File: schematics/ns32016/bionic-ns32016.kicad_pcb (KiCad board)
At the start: 2 copper layers, 66 x 71.1 mm, 17 parts, among them J1 Bionic-P135, J2 Bionic-P245, U1 NS32016N, U2 74HCT126, U3 74HCT541, U4 74HCT541, U5 11AA010-I/TO

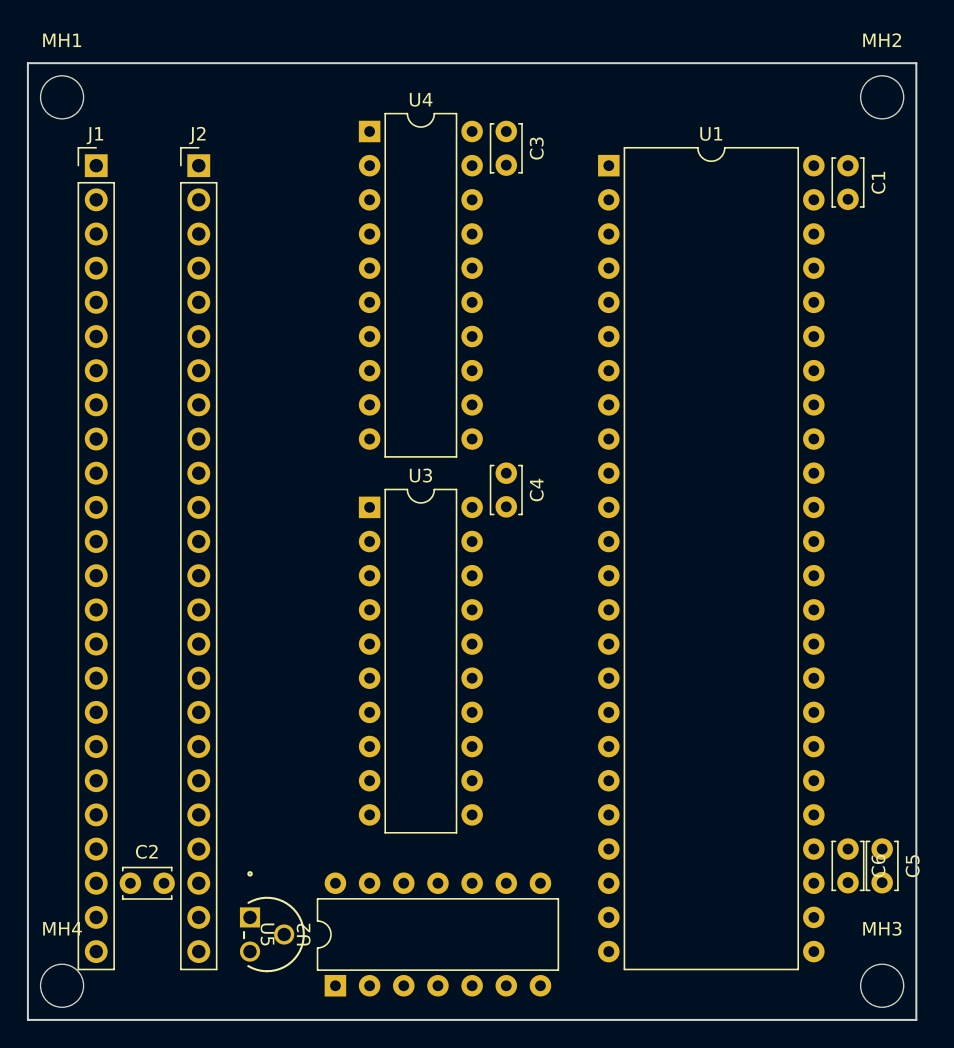
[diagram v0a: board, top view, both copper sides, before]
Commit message: [WIP] [NS32016] Update schematics
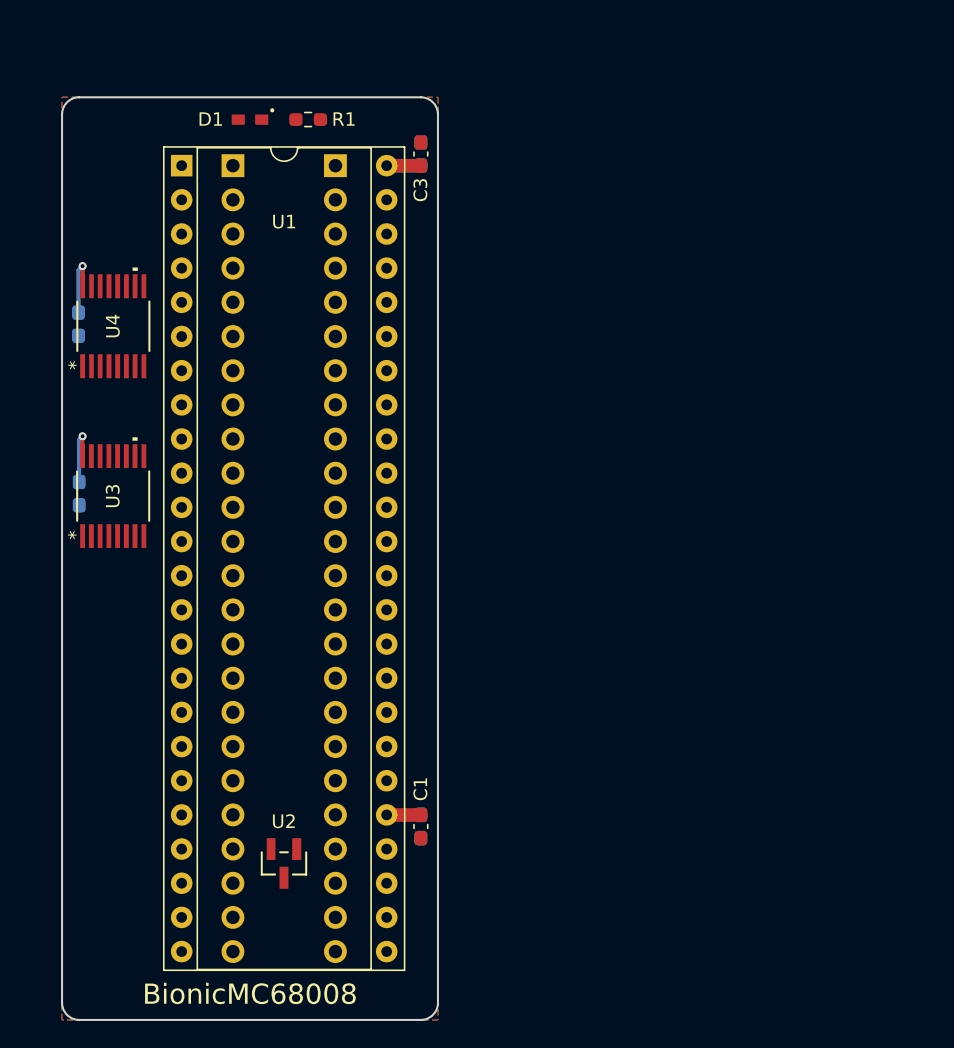
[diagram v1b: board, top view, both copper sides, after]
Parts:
- removed MH1, MH2, MH3, MH4: MountingHole_3.2mm_M3, MountingHole:MountingHole_3.2mm_M3
- removed U5: 11AA010-I/TO, microchip:TO-92_MC_MCH
- added D1: CSL1901UW1, rhom:LED_CSL1901UW1_ROM-M, F.Cu at (115.0, 71.7)
- added R1: 1.6k, Resistor_SMD:R_0603_1608Metric_Pad0.98x0.95mm_HandSolder, F.Cu at (119.3, 71.7)
- C1: value 0.1u -> 1u; footprint Capacitor_THT:C_Disc_D3.4mm_W2.1mm_P2.50mm -> Capacitor_SMD:C_0603_1608Metric_Pad1.08x0.95mm_HandSolder
- C2: value 0.1u -> 1n; footprint Capacitor_THT:C_Disc_D3.4mm_W2.1mm_P2.50mm -> Capacitor_SMD:C_0603_1608Metric_Pad1.08x0.95mm_HandSolder; moved to B.Cu
- C3: footprint Capacitor_THT:C_Disc_D3.4mm_W2.1mm_P2.50mm -> Capacitor_SMD:C_0603_1608Metric_Pad1.08x0.95mm_HandSolder
- C4: value 0.1u -> 22u; footprint Capacitor_THT:C_Disc_D3.4mm_W2.1mm_P2.50mm -> Capacitor_SMD:C_0603_1608Metric_Pad1.08x0.95mm_HandSolder; moved to B.Cu
- C5: value 1000p -> 0.1u; footprint Capacitor_THT:C_Disc_D3.4mm_W2.1mm_P2.50mm -> Capacitor_SMD:C_0603_1608Metric_Pad1.08x0.95mm_HandSolder; moved to B.Cu
- C6: value 1u -> 0.1u; footprint Capacitor_THT:C_Disc_D3.4mm_W2.1mm_P2.50mm -> Capacitor_SMD:C_0603_1608Metric_Pad1.08x0.95mm_HandSolder; moved to B.Cu
- J1: footprint connector:Bionic-P135_Vertical -> bionic:Bionic-P135_Vertical; moved to B.Cu
- J2: footprint connector:Bionic-P245_Vertical -> bionic:Bionic-P245_Vertical; moved to B.Cu
- U1: footprint Package_DIP:DIP-48_W15.24mm -> bionic:DIP-48_W15.24mm_Socket
- U2: value 74HCT126 -> 11AA010-I/TT; footprint Package_DIP:DIP-14_W7.62mm -> microchip:SOT-23_MC_MCH-M
- U3, U4: value 74HCT541 -> 74AHCT157; footprint Package_DIP:DIP-20_W7.62mm -> ti:PW16-M
- moved C6 69.2 mm to (102.2, 86.9)
- moved C5 65.3 mm to (102.3, 99.5)
- moved C1 58.5 mm to (127.7, 124.2)
- moved U1 31.7 mm to (109.9, 75.1)
- moved C4 24.6 mm to (127.7, 74.2), turned to 90 degrees
- moved U4 23.9 mm to (104.8, 87.0), turned to 90 degrees
- moved C2 22.0 mm to (127.7, 124.2), turned to -90 degrees
- moved U3 19.1 mm to (104.8, 99.6), turned to 90 degrees
- moved J1 10.2 mm to (113.7, 75.1), turned to 180 degrees
- moved J2 10.2 mm to (121.3, 75.1), turned to 180 degrees
- moved U2 9.87 mm to (117.5, 126.9), turned to 180 degrees
- moved C3 6.57 mm to (127.7, 74.2), turned to 90 degrees
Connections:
- C1 pad 1: VCC -> Net-(U1-BBG)
- C2 pad 1: VCC -> Net-(U1-BBG)
- C5 pad 1: Net-(U1-BBG) -> VCC
- C6 pad 1: Net-(U1-BBG) -> VCC
- U1 pad 1: Net-(U1-A22) -> /A22
- U1 pad 2: Net-(U1-A21) -> /A21
- U1 pad 26: Net-(U1-PHI1) -> /P46
- U1 pad 27: Net-(U1-PHI2) -> /P47
- U1 pad 3: Net-(U1-A20) -> /A20
- U1 pad 30: /P41 -> /P55
- U1 pad 31: /P45 -> /P54
- U1 pad 32: Net-(U1-~{HBE}) -> /P43
- U1 pad 33: /P50 -> /P41
- U1 pad 36: Net-(U1-U/~{S}) -> /ST4
- U1 pad 38: Net-(U1-~{DDIN}) -> /P42
- U1 pad 39: /P51 -> /ST6
- U1 pad 4: Net-(U1-A19) -> /A19
- U1 pad 40: Net-(U1-ST3) -> /ST3
- U1 pad 41: Net-(U1-ST2) -> /ST2
- U1 pad 42: Net-(U1-ST1) -> /ST1
- U1 pad 43: Net-(U1-ST0) -> /ST0
- U1 pad 44: Net-(U1-~{ILO}) -> /ST5
- U1 pad 45: /P43 -> /P51
- U1 pad 46: /P42 -> /P50
- U1 pad 47: Net-(U1-A23) -> /A23
- U1 pad 5: Net-(U1-A18) -> /A18
- U1 pad 6: Net-(U1-A17) -> /A17
- U1 pad 7: Net-(U1-A16) -> /A16
- U2 pad 1: VCC -> Net-(J2-P57)
- U2 pad 2: /P47 -> VCC
- U2 pad 3: Net-(U1-PHI2) -> GND
- U3 pad 1: /P55 -> /P45
- U3 pad 10: VCC -> /ST6
- U3 pad 11: /P30 -> /A18
- U3 pad 12: /P31 -> /P30
- U3 pad 13: /P32 -> GND
- U3 pad 14: /P33 -> /A19
- U3 pad 15: /P34 -> GND
- U3 pad 16: /P35 -> VCC
- U3 pad 2: Net-(U1-A23) -> /A16
- U3 pad 3: Net-(U1-A22) -> /ST4
- U3 pad 4: Net-(U1-A21) -> /P33
- U3 pad 5: Net-(U1-A20) -> /A17
- U3 pad 6: Net-(U1-A19) -> /ST5
- U3 pad 7: Net-(U1-A18) -> /P32
- U3 pad 8: Net-(U1-A17) -> GND
- U3 pad 9: Net-(U1-A16) -> /P31
- U4 pad 1: /P54 -> /P45
- U4 pad 10: GND -> /ST2
- U4 pad 11: /P37 -> /A22
- U4 pad 12: /P36 -> /P34
- U4 pad 13: /P35 -> /ST3
- U4 pad 14: /P34 -> /A23
- U4 pad 15: /P33 -> GND
- U4 pad 16: /P32 -> VCC
- U4 pad 2: Net-(U1-ST0) -> /A20
- U4 pad 3: Net-(U1-ST1) -> /ST0
- U4 pad 4: Net-(U1-ST2) -> /P37
- U4 pad 5: Net-(U1-ST3) -> /A21
- U4 pad 6: Net-(U1-U/~{S}) -> /ST1
- U4 pad 7: Net-(U1-~{ILO}) -> /P36
- U4 pad 8: Net-(U1-~{DDIN}) -> GND
- U4 pad 9: Net-(U1-~{HBE}) -> /P35
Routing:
- net VCC: track 0.00 -> 15.1 mm, vias 0 -> 2
- net Net-(U1-BBG): track 0.00 -> 5.08 mm
- added copper zone on B.Cu, net GND
- added copper zone on F.Cu, net GND
- added copper zone on In1.Cu, net GND
- added copper zone on In2.Cu, net VCC
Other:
- board size 66 x 71.1 mm -> 27.9 x 68.6 mm
- copper layers 2 -> 4
- rule pad_to_mask_clearance: 0.051 -> 0
- board text added: "BionicMC68008"
- board text added: "JLCJLCJLCJLC"
- board text added: "Rev. 2"

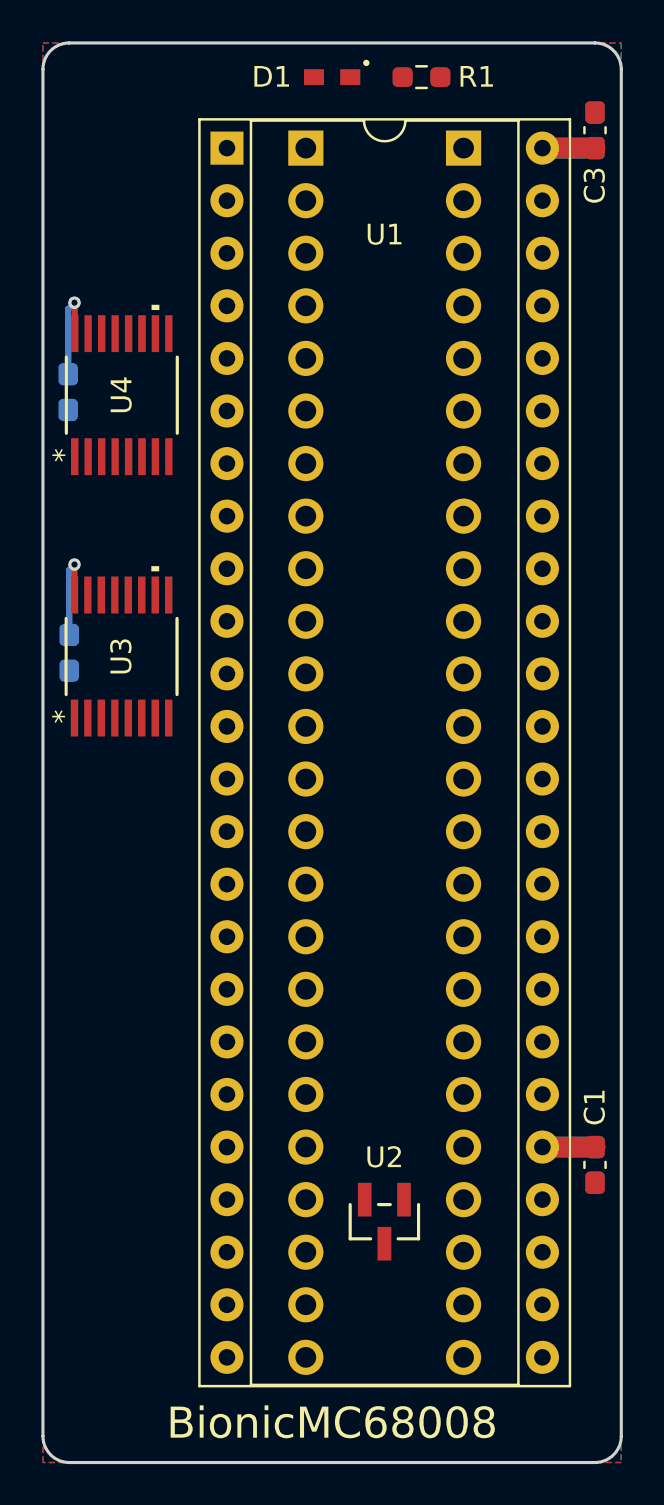
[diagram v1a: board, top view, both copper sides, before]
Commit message: [WIP] [NS32016] Use SMT connector
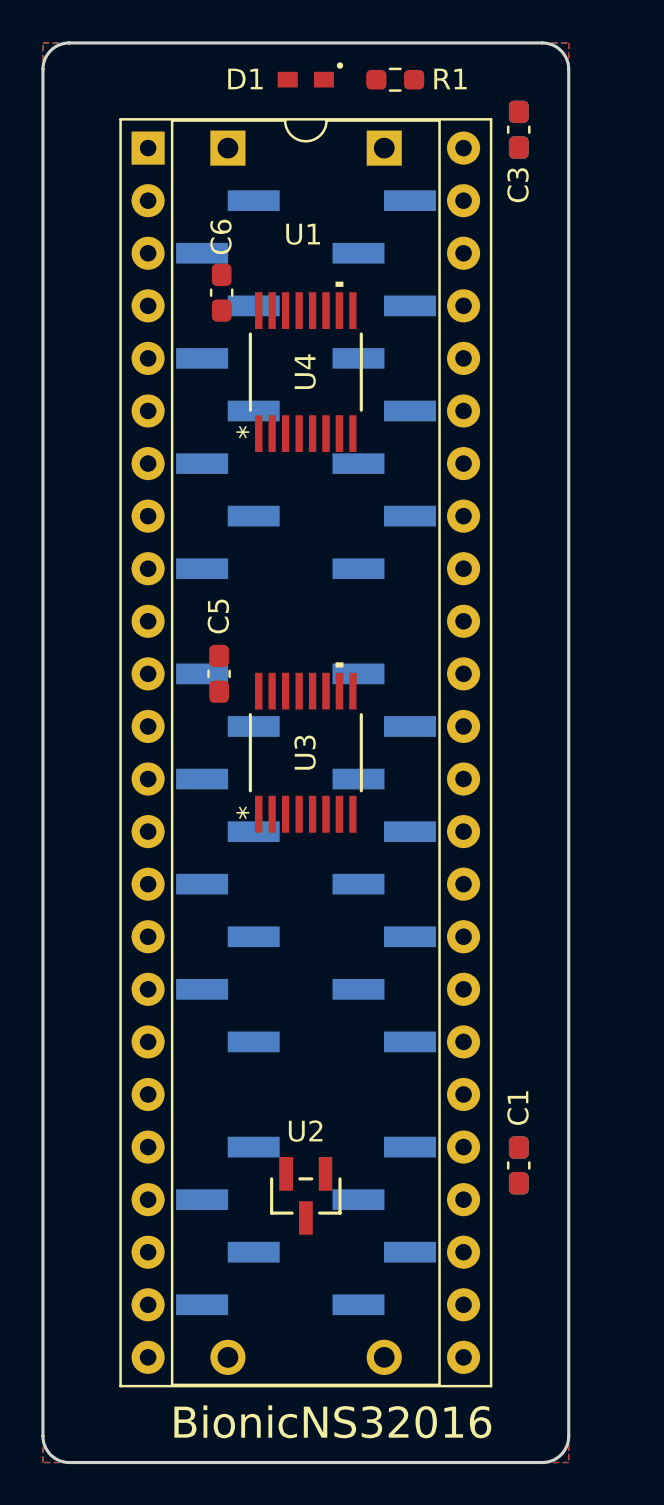
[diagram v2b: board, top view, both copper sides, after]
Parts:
- C5, C6: moved to F.Cu
- J1: footprint bionic:Bionic-P135_Vertical -> bionic:Bionic-P135_SMT
- J2: footprint bionic:Bionic-P245_Vertical -> bionic:Bionic-P245_SMT
- moved J2 29.5 mm to (117.5, 104.3)
- moved J1 29.5 mm to (109.9, 104.3)
- moved U3 10.0 mm to (113.7, 104.3)
- moved U4 8.96 mm to (113.7, 85.9)
- moved C6 8.83 mm to (109.6, 82.1), turned to 90 degrees
- moved C5 7.31 mm to (109.5, 100.5), turned to 90 degrees
- moved U2 3.99 mm to (113.7, 125.7)
- moved U1 3.81 mm to (106.1, 75.1)
- moved C1 3.68 mm to (124.0, 124.2)
- moved C2 3.68 mm to (124.0, 124.2)
- moved C3 3.68 mm to (124.0, 74.2)
- moved C4 3.68 mm to (124.0, 74.2)
- moved D1 1.28 mm to (113.7, 71.8)
- moved R1 1.28 mm to (118.0, 71.8)
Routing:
- net VCC: track 15.1 -> 0.00 mm, vias 2 -> 0
- net Net-(U1-BBG): track 5.08 -> 0.00 mm
- removed copper zone on In1.Cu, net GND
- removed copper zone on In2.Cu, net VCC
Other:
- board size 27.9 x 68.6 mm -> 25.4 x 68.6 mm
- copper layers 4 -> 2
- board text added: "BionicNS32016"
- board text removed: "BionicMC68008"
